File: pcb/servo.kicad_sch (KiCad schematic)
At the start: 7 parts, among them J5 0436500315, Q1 Si3407DV, Q3 NTR4003N

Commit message: Start layout
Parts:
- J3: renamed from J5; footprint (none) -> Connector_Molex:Molex_Micro-Fit_3.0_43650-0315_1x03_P3.00mm_Vertical
- R28: renamed from R22; footprint (none) -> Resistor_SMD:R_0603_1608Metric
- R29: renamed from R23; footprint (none) -> Resistor_SMD:R_0603_1608Metric
- R30: renamed from R21; footprint (none) -> Resistor_SMD:R_0603_1608Metric
- R31: renamed from R20; footprint (none) -> Resistor_SMD:R_0603_1608Metric
- renumbered Q3 to Q4, Q1 to Q5
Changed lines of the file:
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@@
 		(on_board yes)
 		(dnp no)
-		(property "Reference" "R20"
+		(property "Reference" "R31"
 			(at 78.74 43.1799 0)
 			(effects
@@
 			)
 		)
-		(property "Footprint" ""
+		(property "Footprint" "Resistor_SMD:R_0603_1608Metric"
 			(at 76.2 44.45 0)
 			(effects
@@
 			(project ""
 				(path "/1f4fd4ed-9886-4375-a5ac-dc32d5760936/27a1e4e9-ed52-4396-b65c-2ca15ccf5a1d"
-					(reference "R20")
+					(reference "R31")
 					(unit 1)
 				)
@@
 		(dnp no)
 		(fields_autoplaced yes)
-		(property "Reference" "R21"
+		(property "Reference" "R30"
 			(at 69.85 44.45 90)
 			(effects
@@
 			)
 		)
-		(property "Footprint" ""
+		(property "Footprint" "Resistor_SMD:R_0603_1608Metric"
 			(at 69.85 50.8 0)
 			(effects
@@
 			(project ""
 				(path "/1f4fd4ed-9886-4375-a5ac-dc32d5760936/27a1e4e9-ed52-4396-b65c-2ca15ccf5a1d"
-					(reference "R21")
+					(reference "R30")
 					(unit 1)
 				)
@@
 		(dnp no)
 		(fields_autoplaced yes)
-		(property "Reference" "R22"
+		(property "Reference" "R28"
 			(at 44.45 57.15 90)
 			(effects
@@
 			)
 		)
-		(property "Footprint" ""
+		(property "Footprint" "Resistor_SMD:R_0603_1608Metric"
 			(at 44.45 63.5 0)
 			(effects
@@
 			(project "airbrake_mod"
 				(path "/1f4fd4ed-9886-4375-a5ac-dc32d5760936/27a1e4e9-ed52-4396-b65c-2ca15ccf5a1d"
-					(reference "R22")
+					(reference "R28")
 					(unit 1)
 				)
@@
 		(on_board yes)
 		(dnp no)
-		(property "Reference" "R23"
+		(property "Reference" "R29"
 			(at 48.26 68.5799 0)
 			(effects
@@
 			)
 		)
-		(property "Footprint" ""
+		(property "Footprint" "Resistor_SMD:R_0603_1608Metric"
 			(at 50.8 69.85 0)
 			(effects
@@
 			(project "airbrake_mod"
 				(path "/1f4fd4ed-9886-4375-a5ac-dc32d5760936/27a1e4e9-ed52-4396-b65c-2ca15ccf5a1d"
-					(reference "R23")
+					(reference "R29")
 					(unit 1)
 				)
@@
 		(dnp no)
 		(fields_autoplaced yes)
-		(property "Reference" "Q3"
+		(property "Reference" "Q4"
 			(at 67.31 62.2299 0)
 			(effects
@@
 			(project "airbrake_mod"
 				(path "/1f4fd4ed-9886-4375-a5ac-dc32d5760936/27a1e4e9-ed52-4396-b65c-2ca15ccf5a1d"
-					(reference "Q3")
+					(reference "Q4")
 					(unit 1)
 				)
@@
 		(dnp no)
 		(fields_autoplaced yes)
-		(property "Reference" "#PWR046"
+		(property "Reference" "#PWR058"
 			(at 129.54 68.58 0)
 			(effects
@@
 			(project ""
 				(path "/1f4fd4ed-9886-4375-a5ac-dc32d5760936/27a1e4e9-ed52-4396-b65c-2ca15ccf5a1d"
-					(reference "#PWR046")
+					(reference "#PWR058")
 					(unit 1)
 				)
@@
 		(dnp no)
 		(fields_autoplaced yes)
-		(property "Reference" "#PWR050"
+		(property "Reference" "#PWR057"
 			(at 88.9 39.37 0)
 			(effects
@@
 			(project ""
 				(path "/1f4fd4ed-9886-4375-a5ac-dc32d5760936/27a1e4e9-ed52-4396-b65c-2ca15ccf5a1d"
-					(reference "#PWR050")
+					(reference "#PWR057")
 					(unit 1)
 				)
@@
 		(dnp no)
 		(fields_autoplaced yes)
-		(property "Reference" "J5"
+		(property "Reference" "J3"
 			(at 136.525 49.53 0)
 			(effects
@@
 			)
 		)
-		(property "Footprint" ""
+		(property "Footprint" "Connector_Molex:Molex_Micro-Fit_3.0_43650-0315_1x03_P3.00mm_Vertical"
 			(at 137.16 57.15 0)
 			(effects
@@
 			)
 		)
-		(property "Datasheet" "~"
+		(property "Datasheet" "https://www.molex.com/pdm_docs/sd/436500315_sd.pdf"
 			(at 137.16 57.15 0)
 			(effects
@@
 			)
 		)
-		(property "Description" "Generic connector, single row, 01x03, script generated"
+		(property "Description" "Connector Header Through Hole 3 position 0.118\" (3.00mm) Molex Micro Fit"
 			(at 137.16 57.15 0)
 			(effects
@@
 			(project ""
 				(path "/1f4fd4ed-9886-4375-a5ac-dc32d5760936/27a1e4e9-ed52-4396-b65c-2ca15ccf5a1d"
-					(reference "J5")
+					(reference "J3")
 					(unit 1)
 				)
@@
 		(on_board yes)
 		(dnp no)
-		(property "Reference" "Q1"
+		(property "Reference" "Q5"
 			(at 91.44 49.53 0)
 			(effects
@@
 			(project ""
 				(path "/1f4fd4ed-9886-4375-a5ac-dc32d5760936/27a1e4e9-ed52-4396-b65c-2ca15ccf5a1d"
-					(reference "Q1")
+					(reference "Q5")
 					(unit 1)
 				)
@@
 		(dnp no)
 		(fields_autoplaced yes)
-		(property "Reference" "#PWR051"
+		(property "Reference" "#PWR056"
 			(at 63.5 82.55 0)
 			(effects
@@
 			(project ""
 				(path "/1f4fd4ed-9886-4375-a5ac-dc32d5760936/27a1e4e9-ed52-4396-b65c-2ca15ccf5a1d"
-					(reference "#PWR051")
-					(unit 1)
-				)
+					(reference "#PWR056")
+					(unit 1)
+				)

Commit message: Layout power
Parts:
- added TP1, TP2, TP3, TP4: RCUCTE, TestPoint_KOASpeer:TestPoint_Chip_RCUCTE_0603, symbol Connector:TestPoint
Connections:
- net PWM: now also TP3.1
- net SERVO_PWR: now also TP4.1
- net at Q5.3 (G), R30.2, R31.2: now also TP2.1
- net at Q4.1 (G), R28.2, R29.1: now also TP1.1

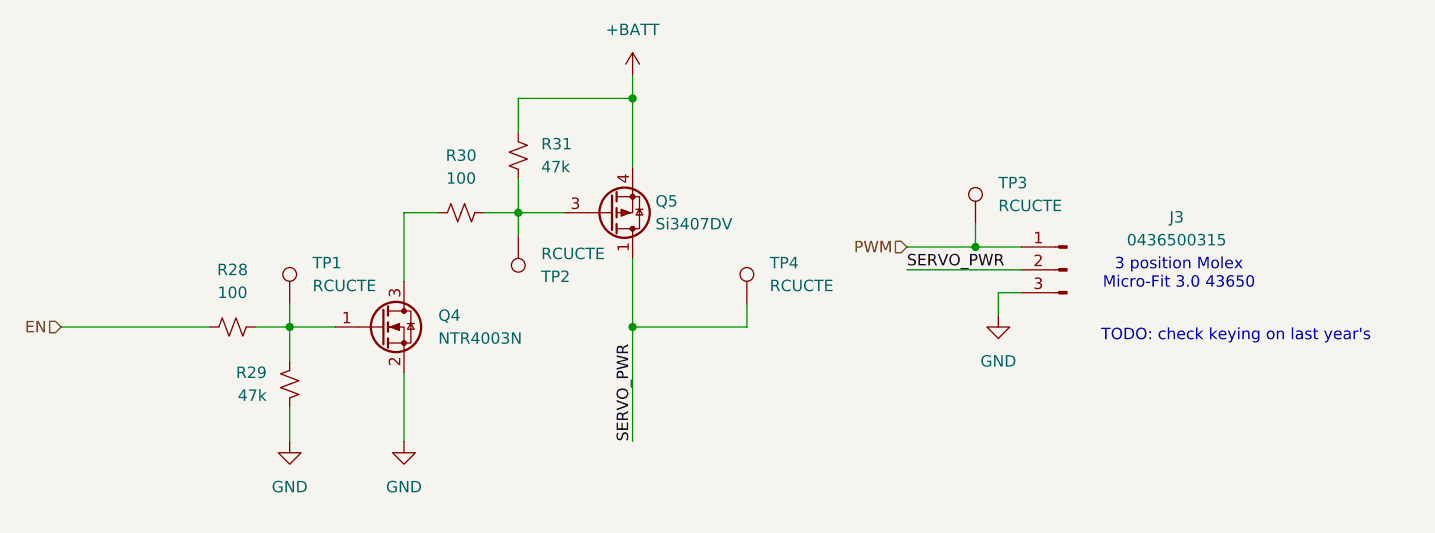
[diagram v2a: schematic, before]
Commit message: Layout MCU decoupling
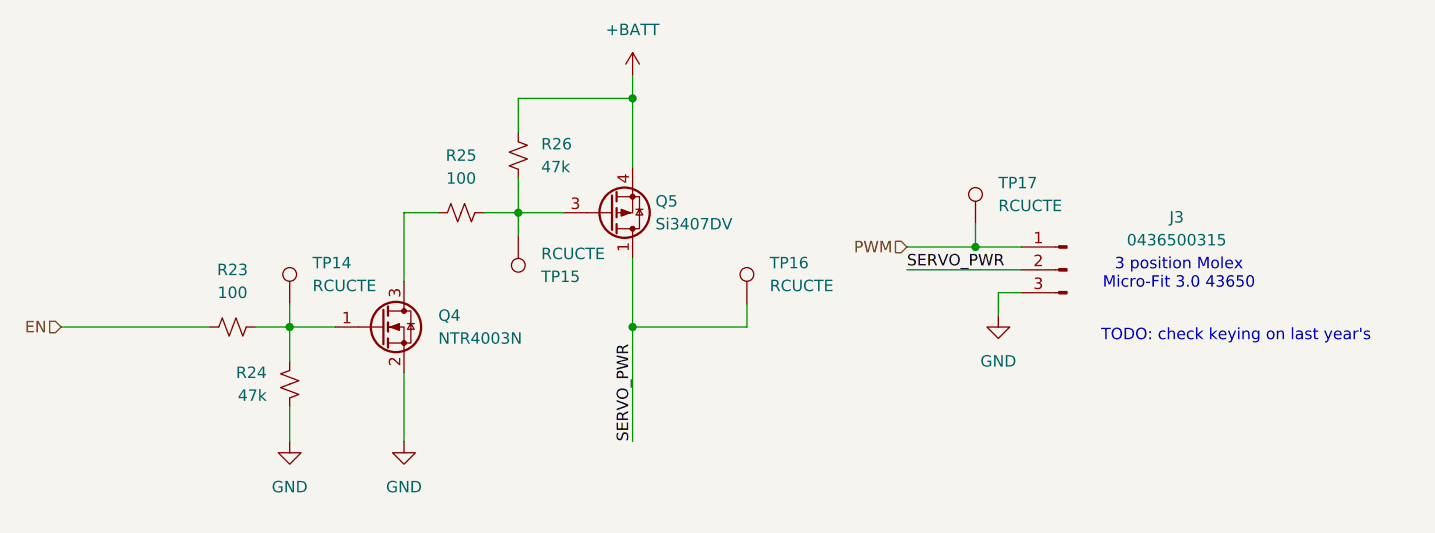
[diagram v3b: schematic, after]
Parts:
- renumbered R28 to R23, R29 to R24, R30 to R25, R31 to R26, TP1 to TP14, TP2 to TP15, TP4 to TP16, TP3 to TP17
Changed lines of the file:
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@@
 		(on_board yes)
 		(dnp no)
-		(property "Reference" "TP2"
+		(property "Reference" "TP15"
 			(at 78.74 57.9121 0)
 			(effects
@@
 			(project "airbrake_mod"
 				(path "/1f4fd4ed-9886-4375-a5ac-dc32d5760936/27a1e4e9-ed52-4396-b65c-2ca15ccf5a1d"
-					(reference "TP2")
+					(reference "TP15")
 					(unit 1)
 				)
@@
 		(on_board yes)
 		(dnp no)
-		(property "Reference" "R31"
+		(property "Reference" "R26"
 			(at 78.74 43.1799 0)
 			(effects
@@
 			(project ""
 				(path "/1f4fd4ed-9886-4375-a5ac-dc32d5760936/27a1e4e9-ed52-4396-b65c-2ca15ccf5a1d"
-					(reference "R31")
+					(reference "R26")
 					(unit 1)
 				)
@@
 		(on_board yes)
 		(dnp no)
-		(property "Reference" "TP1"
+		(property "Reference" "TP14"
 			(at 53.34 56.3879 0)
 			(effects
@@
 			(project ""
 				(path "/1f4fd4ed-9886-4375-a5ac-dc32d5760936/27a1e4e9-ed52-4396-b65c-2ca15ccf5a1d"
-					(reference "TP1")
+					(reference "TP14")
 					(unit 1)
 				)
@@
 		(dnp no)
 		(fields_autoplaced yes)
-		(property "Reference" "R30"
+		(property "Reference" "R25"
 			(at 69.85 44.45 90)
 			(effects
@@
 			(project ""
 				(path "/1f4fd4ed-9886-4375-a5ac-dc32d5760936/27a1e4e9-ed52-4396-b65c-2ca15ccf5a1d"
-					(reference "R30")
+					(reference "R25")
 					(unit 1)
 				)
@@
 		(dnp no)
 		(fields_autoplaced yes)
-		(property "Reference" "R28"
+		(property "Reference" "R23"
 			(at 44.45 57.15 90)
 			(effects
@@
 			(project "airbrake_mod"
 				(path "/1f4fd4ed-9886-4375-a5ac-dc32d5760936/27a1e4e9-ed52-4396-b65c-2ca15ccf5a1d"
-					(reference "R28")
+					(reference "R23")
 					(unit 1)
 				)
@@
 		(on_board yes)
 		(dnp no)
-		(property "Reference" "R29"
+		(property "Reference" "R24"
 			(at 48.26 68.5799 0)
 			(effects
@@
 			(project "airbrake_mod"
 				(path "/1f4fd4ed-9886-4375-a5ac-dc32d5760936/27a1e4e9-ed52-4396-b65c-2ca15ccf5a1d"
-					(reference "R29")
+					(reference "R24")
 					(unit 1)
 				)
@@
 		(on_board yes)
 		(dnp no)
-		(property "Reference" "TP4"
+		(property "Reference" "TP16"
 			(at 104.14 56.3879 0)
 			(effects
@@
 			(project "airbrake_mod"
 				(path "/1f4fd4ed-9886-4375-a5ac-dc32d5760936/27a1e4e9-ed52-4396-b65c-2ca15ccf5a1d"
-					(reference "TP4")
+					(reference "TP16")
 					(unit 1)
 				)
@@
 		(on_board yes)
 		(dnp no)
-		(property "Reference" "TP3"
+		(property "Reference" "TP17"
 			(at 129.54 47.4979 0)
 			(effects
@@
 			(project "airbrake_mod"
 				(path "/1f4fd4ed-9886-4375-a5ac-dc32d5760936/27a1e4e9-ed52-4396-b65c-2ca15ccf5a1d"
-					(reference "TP3")
-					(unit 1)
-				)
+					(reference "TP17")
+					(unit 1)
+				)

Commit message: Incorporate feedback servo with 4 pin molex and additional ADC channel
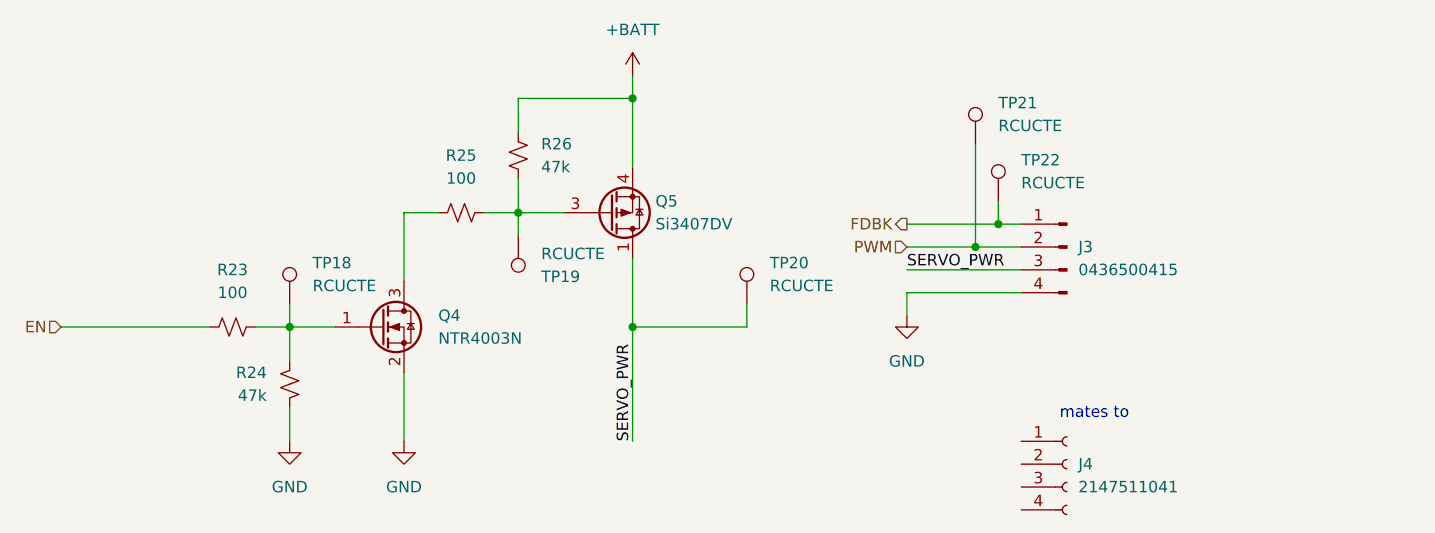
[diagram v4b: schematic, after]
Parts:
- removed J3: 0436500315, Connector_Molex:Molex_Micro-Fit_3.0_43650-0315_1x03_P3.00mm_Vertical, symbol Connector:Conn_01x03_Pin
- added J3: 0436500415, Connector_Molex:Molex_Micro-Fit_3.0_43650-0415_1x04_P3.00mm_Vertical, symbol Connector:Conn_01x04_Pin
- added J4: 2147511041, symbol Connector:Conn_01x04_Socket
- added TP22: RCUCTE, TestPoint_KOASpeer:TestPoint_Chip_RCUCTE_0603, symbol Connector:TestPoint
- renumbered TP14 to TP18, TP15 to TP19, TP16 to TP20, TP17 to TP21
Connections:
- net GND: now also J3.4 (Pin_4)
- net PWM: now also J3.2 (Pin_2)
- net SERVO_PWR: now also J3.3 (Pin_3)
- new net FDBK: J3.1 (Pin_1), TP22.1
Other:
- note added: "mates to"
- note removed: "3 position Molex Micro-Fit 3.0 43650"
- note removed: "TODO: check keying on last year's"
- moved on the sheet: TP21

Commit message: Add CUR schematic sheet title block
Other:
- company: (none) -> Clarkson University Rocketry Team
- title: (none) -> Air Brakes Module
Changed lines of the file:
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@@
 	(generator_version "9.0")
 	(paper "A4")
+	(title_block
+		(title "Air Brakes Module")
+		(date "2025-11-23")
+		(company "Clarkson University Rocketry Team")
+	)
 	(text "mates to"
 		(exclude_from_sim no)
